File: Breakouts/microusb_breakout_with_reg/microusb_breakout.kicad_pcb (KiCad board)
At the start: 2 copper layers, 8 x 11 mm, 5 parts, among them J1 USB_B_Micro, J2 USB, U1 AMS1117-3.3

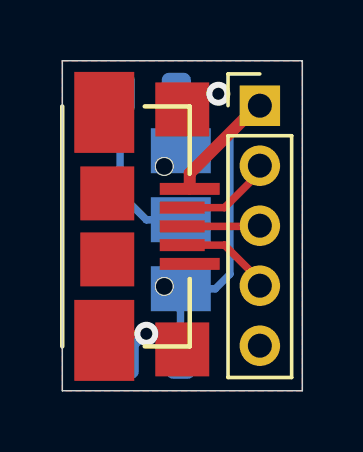
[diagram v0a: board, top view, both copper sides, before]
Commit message: Fixing the microusb_breakout_with_reg board bug and removing the README disclaimer
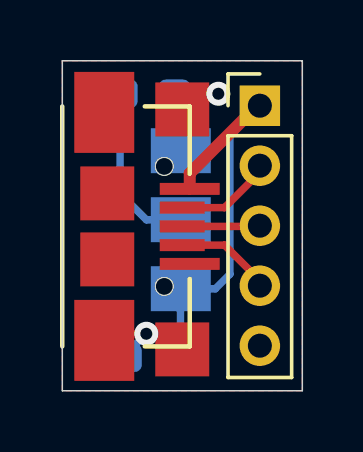
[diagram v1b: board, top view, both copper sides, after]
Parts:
- C1, C2: footprint Capacitor_SMD:C_0805_2012Metric -> Capacitor_SMD:C_0603_1608Metric_Pad1.05x0.95mm_HandSolder
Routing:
- net Net-(C1-Pad2): track 5.42 -> 7.38 mm
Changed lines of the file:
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@@
-(kicad_pcb (version 20171130) (host pcbnew "(5.1.2)-1")
+(kicad_pcb (version 20171130) (host pcbnew 5.1.5+dfsg1-2build2)
   (general
     (thickness 1.6)
     (drawings 4)
-    (tracks 30)
+    (tracks 32)
     (zones 0)
     (modules 5)
@@
     (add_net "Net-(J1-Pad4)")
   )
+  (module Capacitor_SMD:C_0603_1608Metric_Pad1.05x0.95mm_HandSolder (layer B.Cu)
+    (at 182.8625 117.6)
+    (descr "Capacitor SMD 0603 (1608 Metric), square (rectangular) end terminal, IPC_7351 nominal with elongated pad for handsoldering. (Body size source: http://www.tortai-tech.com/upload/download/2011102023233369053.pdf), generated with kicad-footprint-generator")
+    (tags "capacitor handsolder")
+    (attr smd)
+    (fp_text reference C2 (at 0 1.65) (layer B.SilkS) hide
+      (effects (font (size 1 1) (thickness 0.15)) (justify mirror))
+    )
+    (fp_text value 100n (at 0 -1.65) (layer B.Fab)
+      (effects (font (size 1 1) (thickness 0.15)) (justify mirror))
+    )
+    (fp_text user %R (at 0 0) (layer B.Fab)
+      (effects (font (size 0.5 0.5) (thickness 0.08)) (justify mirror))
+    )
+    (fp_line (start 1.65 -0.73) (end -1.65 -0.73) (layer B.CrtYd) (width 0.05))
+    (fp_line (start 1.65 0.73) (end 1.65 -0.73) (layer B.CrtYd) (width 0.05))
+    (fp_line (start -1.65 0.73) (end 1.65 0.73) (layer B.CrtYd) (width 0.05))
+    (fp_line (start -1.65 -0.73) (end -1.65 0.73) (layer B.CrtYd) (width 0.05))
+    (fp_line (start -0.171267 -0.51) (end 0.171267 -0.51) (layer B.SilkS) (width 0.12))
+    (fp_line (start -0.171267 0.51) (end 0.171267 0.51) (layer B.SilkS) (width 0.12))
+    (fp_line (start 0.8 -0.4) (end -0.8 -0.4) (layer B.Fab) (width 0.1))
+    (fp_line (start 0.8 0.4) (end 0.8 -0.4) (layer B.Fab) (width 0.1))
+    (fp_line (start -0.8 0.4) (end 0.8 0.4) (layer B.Fab) (width 0.1))
+    (fp_line (start -0.8 -0.4) (end -0.8 0.4) (layer B.Fab) (width 0.1))
+    (pad 2 smd roundrect (at 0.875 0) (size 1.05 0.95) (layers B.Cu B.Paste B.Mask) (roundrect_rratio 0.25)
+      (net 4 "Net-(C1-Pad2)"))
+    (pad 1 smd roundrect (at -0.875 0) (size 1.05 0.95) (layers B.Cu B.Paste B.Mask) (roundrect_rratio 0.25)
+      (net 6 "Net-(C2-Pad1)"))
+    (model ${KISYS3DMOD}/Capacitor_SMD.3dshapes/C_0603_1608Metric.wrl
+      (at (xyz 0 0 0))
+      (scale (xyz 1 1 1))
+      (rotate (xyz 0 0 0))
+    )
+  )
+  (module Capacitor_SMD:C_0603_1608Metric_Pad1.05x0.95mm_HandSolder (layer B.Cu)
+    (at 183 126.4 180)
+    (descr "Capacitor SMD 0603 (1608 Metric), square (rectangular) end terminal, IPC_7351 nominal with elongated pad for handsoldering. (Body size source: http://www.tortai-tech.com/upload/download/2011102023233369053.pdf), generated with kicad-footprint-generator")
+    (tags "capacitor handsolder")
+    (attr smd)
+    (fp_text reference C1 (at 0 1.65) (layer B.SilkS) hide
+      (effects (font (size 1 1) (thickness 0.15)) (justify mirror))
+    )
+    (fp_text value 100n (at 0 -1.65) (layer B.Fab)
+      (effects (font (size 1 1) (thickness 0.15)) (justify mirror))
+    )
+    (fp_text user %R (at 0 0) (layer B.Fab)
+      (effects (font (size 0.5 0.5) (thickness 0.08)) (justify mirror))
+    )
+    (fp_line (start 1.65 -0.73) (end -1.65 -0.73) (layer B.CrtYd) (width 0.05))
+    (fp_line (start 1.65 0.73) (end 1.65 -0.73) (layer B.CrtYd) (width 0.05))
+    (fp_line (start -1.65 0.73) (end 1.65 0.73) (layer B.CrtYd) (width 0.05))
+    (fp_line (start -1.65 -0.73) (end -1.65 0.73) (layer B.CrtYd) (width 0.05))
+    (fp_line (start -0.171267 -0.51) (end 0.171267 -0.51) (layer B.SilkS) (width 0.12))
+    (fp_line (start -0.171267 0.51) (end 0.171267 0.51) (layer B.SilkS) (width 0.12))
+    (fp_line (start 0.8 -0.4) (end -0.8 -0.4) (layer B.Fab) (width 0.1))
+    (fp_line (start 0.8 0.4) (end 0.8 -0.4) (layer B.Fab) (width 0.1))
+    (fp_line (start -0.8 0.4) (end 0.8 0.4) (layer B.Fab) (width 0.1))
+    (fp_line (start -0.8 -0.4) (end -0.8 0.4) (layer B.Fab) (width 0.1))
+    (pad 2 smd roundrect (at 0.875 0 180) (size 1.05 0.95) (layers B.Cu B.Paste B.Mask) (roundrect_rratio 0.25)
+      (net 4 "Net-(C1-Pad2)"))
+    (pad 1 smd roundrect (at -0.875 0 180) (size 1.05 0.95) (layers B.Cu B.Paste B.Mask) (roundrect_rratio 0.25)
+      (net 5 "Net-(C1-Pad1)"))
+    (model ${KISYS3DMOD}/Capacitor_SMD.3dshapes/C_0603_1608Metric.wrl
+      (at (xyz 0 0 0))
+      (scale (xyz 1 1 1))
+      (rotate (xyz 0 0 0))
+    )
+  )
   (module Package_TO_SOT_SMD:SOT-223-3_TabPin2 (layer B.Cu)
     (at 180.8 121.8 180)
@@
       (net 6 "Net-(C2-Pad1)"))
     (model ${KISYS3DMOD}/Package_TO_SOT_SMD.3dshapes/SOT-223.wrl
-      (at (xyz 0 0 0))
-      (scale (xyz 1 1 1))
-      (rotate (xyz 0 0 0))
-    )
-  )
-  (module Capacitor_SMD:C_0805_2012Metric (layer B.Cu)
-    (at 182.8625 117.6)
-    (descr "Capacitor SMD 0805 (2012 Metric), square (rectangular) end terminal, IPC_7351 nominal, (Body size source: https://docs.google.com/spreadsheets/d/1BsfQQcO9C6DZCsRaXUlFlo91Tg2WpOkGARC1WS5S8t0/edit?usp=sharing), generated with kicad-footprint-generator")
-    (tags capacitor)
-    (attr smd)
-    (fp_text reference C2 (at 0 1.65) (layer B.SilkS) hide
-      (effects (font (size 1 1) (thickness 0.15)) (justify mirror))
-    )
-    (fp_text value 100n (at 0 -1.65) (layer B.Fab)
-      (effects (font (size 1 1) (thickness 0.15)) (justify mirror))
-    )
-    (fp_text user %R (at 0 0) (layer B.Fab)
-      (effects (font (size 0.5 0.5) (thickness 0.08)) (justify mirror))
-    )
-    (fp_line (start 1.68 -0.95) (end -1.68 -0.95) (layer B.CrtYd) (width 0.05))
-    (fp_line (start 1.68 0.95) (end 1.68 -0.95) (layer B.CrtYd) (width 0.05))
-    (fp_line (start -1.68 0.95) (end 1.68 0.95) (layer B.CrtYd) (width 0.05))
-    (fp_line (start -1.68 -0.95) (end -1.68 0.95) (layer B.CrtYd) (width 0.05))
-    (fp_line (start -0.258578 -0.71) (end 0.258578 -0.71) (layer B.SilkS) (width 0.12))
-    (fp_line (start -0.258578 0.71) (end 0.258578 0.71) (layer B.SilkS) (width 0.12))
-    (fp_line (start 1 -0.6) (end -1 -0.6) (layer B.Fab) (width 0.1))
-    (fp_line (start 1 0.6) (end 1 -0.6) (layer B.Fab) (width 0.1))
-    (fp_line (start -1 0.6) (end 1 0.6) (layer B.Fab) (width 0.1))
-    (fp_line (start -1 -0.6) (end -1 0.6) (layer B.Fab) (width 0.1))
-    (pad 2 smd roundrect (at 0.9375 0) (size 0.975 1.4) (layers B.Cu B.Paste B.Mask) (roundrect_rratio 0.25)
-      (net 4 "Net-(C1-Pad2)"))
-    (pad 1 smd roundrect (at -0.9375 0) (size 0.975 1.4) (layers B.Cu B.Paste B.Mask) (roundrect_rratio 0.25)
-      (net 6 "Net-(C2-Pad1)"))
-    (model ${KISYS3DMOD}/Capacitor_SMD.3dshapes/C_0805_2012Metric.wrl
-      (at (xyz 0 0 0))
-      (scale (xyz 1 1 1))
-      (rotate (xyz 0 0 0))
-    )
-  )
-  (module Capacitor_SMD:C_0805_2012Metric (layer B.Cu)
-    (at 183 126.4 180)
-    (descr "Capacitor SMD 0805 (2012 Metric), square (rectangular) end terminal, IPC_7351 nominal, (Body size source: https://docs.google.com/spreadsheets/d/1BsfQQcO9C6DZCsRaXUlFlo91Tg2WpOkGARC1WS5S8t0/edit?usp=sharing), generated with kicad-footprint-generator")
-    (tags capacitor)
-    (attr smd)
-    (fp_text reference C1 (at 0 1.65) (layer B.SilkS) hide
-      (effects (font (size 1 1) (thickness 0.15)) (justify mirror))
-    )
-    (fp_text value 100n (at 0 -1.65) (layer B.Fab)
-      (effects (font (size 1 1) (thickness 0.15)) (justify mirror))
-    )
-    (fp_text user %R (at 0 0) (layer B.Fab)
-      (effects (font (size 0.5 0.5) (thickness 0.08)) (justify mirror))
-    )
-    (fp_line (start 1.68 -0.95) (end -1.68 -0.95) (layer B.CrtYd) (width 0.05))
-    (fp_line (start 1.68 0.95) (end 1.68 -0.95) (layer B.CrtYd) (width 0.05))
-    (fp_line (start -1.68 0.95) (end 1.68 0.95) (layer B.CrtYd) (width 0.05))
-    (fp_line (start -1.68 -0.95) (end -1.68 0.95) (layer B.CrtYd) (width 0.05))
-    (fp_line (start -0.258578 -0.71) (end 0.258578 -0.71) (layer B.SilkS) (width 0.12))
-    (fp_line (start -0.258578 0.71) (end 0.258578 0.71) (layer B.SilkS) (width 0.12))
-    (fp_line (start 1 -0.6) (end -1 -0.6) (layer B.Fab) (width 0.1))
-    (fp_line (start 1 0.6) (end 1 -0.6) (layer B.Fab) (width 0.1))
-    (fp_line (start -1 0.6) (end 1 0.6) (layer B.Fab) (width 0.1))
-    (fp_line (start -1 -0.6) (end -1 0.6) (layer B.Fab) (width 0.1))
-    (pad 2 smd roundrect (at 0.9375 0 180) (size 0.975 1.4) (layers B.Cu B.Paste B.Mask) (roundrect_rratio 0.25)
-      (net 4 "Net-(C1-Pad2)"))
-    (pad 1 smd roundrect (at -0.9375 0 180) (size 0.975 1.4) (layers B.Cu B.Paste B.Mask) (roundrect_rratio 0.25)
-      (net 5 "Net-(C1-Pad1)"))
-    (model ${KISYS3DMOD}/Capacitor_SMD.3dshapes/C_0805_2012Metric.wrl
       (at (xyz 0 0 0))
       (scale (xyz 1 1 1))
@@
   (segment (start 181.6192 125.6) (end 181.3976 125.8216) (width 0.25) (layer F.Cu) (net 4))
   (segment (start 182.8 125.6) (end 181.6192 125.6) (width 0.25) (layer F.Cu) (net 4))
+  (segment (start 183.8 119.35) (end 183.95 119.5) (width 0.25) (layer B.Cu) (net 4))
+  (segment (start 183.8 117.6) (end 183.8 119.35) (width 0.25) (layer B.Cu) (net 4))
   (segment (start 184.2476 120.2524) (end 184.2476 120.7716) (width 0.4) (layer F.Cu) (net 5))
   (segment (start 186.584201 117.9984) (end 186.5016 117.9984) (width 0.25) (layer F.Cu) (net 5))
